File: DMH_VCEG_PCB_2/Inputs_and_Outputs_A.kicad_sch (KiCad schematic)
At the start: 35 parts, among them J1 TS_Jack_6.35mm_Sw, J10 TS_Jack_6.35mm_Sw, J2 TS_Jack_6.35mm_Sw, J200 IDC_02x08, J21 Conn_01x10_PinHeader, J22 Conn_01x10_PinHeader, J23 Conn_01x10_PinHeader, J27 Conn_01x06_PinHeader, J3 TS_Jack_6.35mm_Sw, J4 TS_Jack_6.35mm_Sw, J5 TS_Jack_6.35mm_Sw, J6 TS_Jack_6.35mm_Sw, J7 TS_Jack_6.35mm_Sw, J8 TS_Jack_6.35mm_Sw, J9 TS_Jack_6.35mm_Sw, U21 TL072, U9 TL074

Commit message: Placed ICs and pin headers on PCB 2
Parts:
- J21, J22, J23: footprint Connector_PinHeader_2.54mm:PinHeader_1x10_P2.54mm_Vertical -> Connector_PinSocket_2.54mm:PinSocket_1x10_P2.54mm_Vertical
- J27: footprint Connector_PinHeader_2.54mm:PinHeader_1x06_P2.54mm_Vertical -> Connector_PinSocket_2.54mm:PinSocket_1x06_P2.54mm_Vertical
- J27: footprint (none) -> Connector_PinSocket_2.54mm:PinSocket_1x06_P2.54mm_Vertical
- U21: footprint Package_DIP:DIP-8_W7.62mm -> Package_DIP:DIP-8_W7.62mm_Socket
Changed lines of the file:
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@@
 			)
 		)
-		(property "Footprint" "Connector_PinHeader_2.54mm:PinHeader_1x10_P2.54mm_Vertical"
+		(property "Footprint" "Connector_PinSocket_2.54mm:PinSocket_1x10_P2.54mm_Vertical"
 			(at 146.05 124.46 0)
 			(effects
@@
 			)
 		)
-		(property "Footprint" "Connector_PinHeader_2.54mm:PinHeader_1x10_P2.54mm_Vertical"
+		(property "Footprint" "Connector_PinSocket_2.54mm:PinSocket_1x10_P2.54mm_Vertical"
 			(at 190.5 179.07 0)
 			(effects
@@
 			)
 		)
-		(property "Footprint" "Connector_PinHeader_2.54mm:PinHeader_1x10_P2.54mm_Vertical"
+		(property "Footprint" "Connector_PinSocket_2.54mm:PinSocket_1x10_P2.54mm_Vertical"
 			(at 146.05 29.21 0)
 			(effects
@@
 			)
 		)
-		(property "Footprint" "Connector_PinHeader_2.54mm:PinHeader_1x10_P2.54mm_Vertical"
+		(property "Footprint" "Connector_PinSocket_2.54mm:PinSocket_1x10_P2.54mm_Vertical"
 			(at 190.5 163.83 0)
 			(effects
@@
 			)
 		)
-		(property "Footprint" "Connector_PinHeader_2.54mm:PinHeader_1x06_P2.54mm_Vertical"
+		(property "Footprint" "Connector_PinSocket_2.54mm:PinSocket_1x06_P2.54mm_Vertical"
 			(at 107.95 223.52 0)
 			(effects
@@
 			)
 		)
-		(property "Footprint" "Connector_PinHeader_2.54mm:PinHeader_1x10_P2.54mm_Vertical"
+		(property "Footprint" "Connector_PinSocket_2.54mm:PinSocket_1x10_P2.54mm_Vertical"
 			(at 190.5 151.13 0)
 			(effects
@@
 			)
 		)
-		(property "Footprint" "Connector_PinHeader_2.54mm:PinHeader_1x10_P2.54mm_Vertical"
+		(property "Footprint" "Connector_PinSocket_2.54mm:PinSocket_1x10_P2.54mm_Vertical"
 			(at 88.9 90.17 0)
 			(effects
@@
 			)
 		)
-		(property "Footprint" ""
+		(property "Footprint" "Connector_PinSocket_2.54mm:PinSocket_1x06_P2.54mm_Vertical"
 			(at 190.5 189.23 0)
 			(effects
@@
 			)
 		)
-		(property "Footprint" "Connector_PinHeader_2.54mm:PinHeader_1x10_P2.54mm_Vertical"
+		(property "Footprint" "Connector_PinSocket_2.54mm:PinSocket_1x10_P2.54mm_Vertical"
 			(at 190.5 176.53 0)
 			(effects
@@
 			)
 		)
-		(property "Footprint" "Connector_PinHeader_2.54mm:PinHeader_1x06_P2.54mm_Vertical"
+		(property "Footprint" "Connector_PinSocket_2.54mm:PinSocket_1x06_P2.54mm_Vertical"
 			(at 177.8 220.98 0)
 			(effects
@@
 			)
 		)
-		(property "Footprint" "Connector_PinHeader_2.54mm:PinHeader_1x10_P2.54mm_Vertical"
+		(property "Footprint" "Connector_PinSocket_2.54mm:PinSocket_1x10_P2.54mm_Vertical"
 			(at 88.9 58.42 0)
 			(effects
@@
 			)
 		)
-		(property "Footprint" "Connector_PinHeader_2.54mm:PinHeader_1x10_P2.54mm_Vertical"
+		(property "Footprint" "Connector_PinSocket_2.54mm:PinSocket_1x10_P2.54mm_Vertical"
 			(at 88.9 121.92 0)
 			(effects
@@
 			)
 		)
-		(property "Footprint" "Connector_PinHeader_2.54mm:PinHeader_1x10_P2.54mm_Vertical"
+		(property "Footprint" "Connector_PinSocket_2.54mm:PinSocket_1x10_P2.54mm_Vertical"
 			(at 88.9 26.67 0)
 			(effects
@@
 			)
 		)
-		(property "Footprint" "Connector_PinHeader_2.54mm:PinHeader_1x10_P2.54mm_Vertical"
+		(property "Footprint" "Connector_PinSocket_2.54mm:PinSocket_1x10_P2.54mm_Vertical"
 			(at 146.05 60.96 0)
 			(effects
@@
 			)
 		)
-		(property "Footprint" "Connector_PinHeader_2.54mm:PinHeader_1x10_P2.54mm_Vertical"
+		(property "Footprint" "Connector_PinSocket_2.54mm:PinSocket_1x10_P2.54mm_Vertical"
 			(at 190.5 153.67 0)
 			(effects
@@
 			)
 		)
-		(property "Footprint" ""
+		(property "Footprint" "Connector_PinSocket_2.54mm:PinSocket_1x06_P2.54mm_Vertical"
 			(at 190.5 191.77 0)
 			(effects
@@
 			)
 		)
-		(property "Footprint" "Connector_PinHeader_2.54mm:PinHeader_1x10_P2.54mm_Vertical"
+		(property "Footprint" "Connector_PinSocket_2.54mm:PinSocket_1x10_P2.54mm_Vertical"
 			(at 146.05 92.71 0)
 			(effects
@@
 			)
 		)
-		(property "Footprint" "Package_DIP:DIP-8_W7.62mm"
+		(property "Footprint" "Package_DIP:DIP-8_W7.62mm_Socket"
 			(at 146.05 228.6 0)
 			(effects
@@
 			)
 		)
-		(property "Footprint" "Connector_PinHeader_2.54mm:PinHeader_1x10_P2.54mm_Vertical"
+		(property "Footprint" "Connector_PinSocket_2.54mm:PinSocket_1x10_P2.54mm_Vertical"
 			(at 190.5 166.37 0)
 			(effects

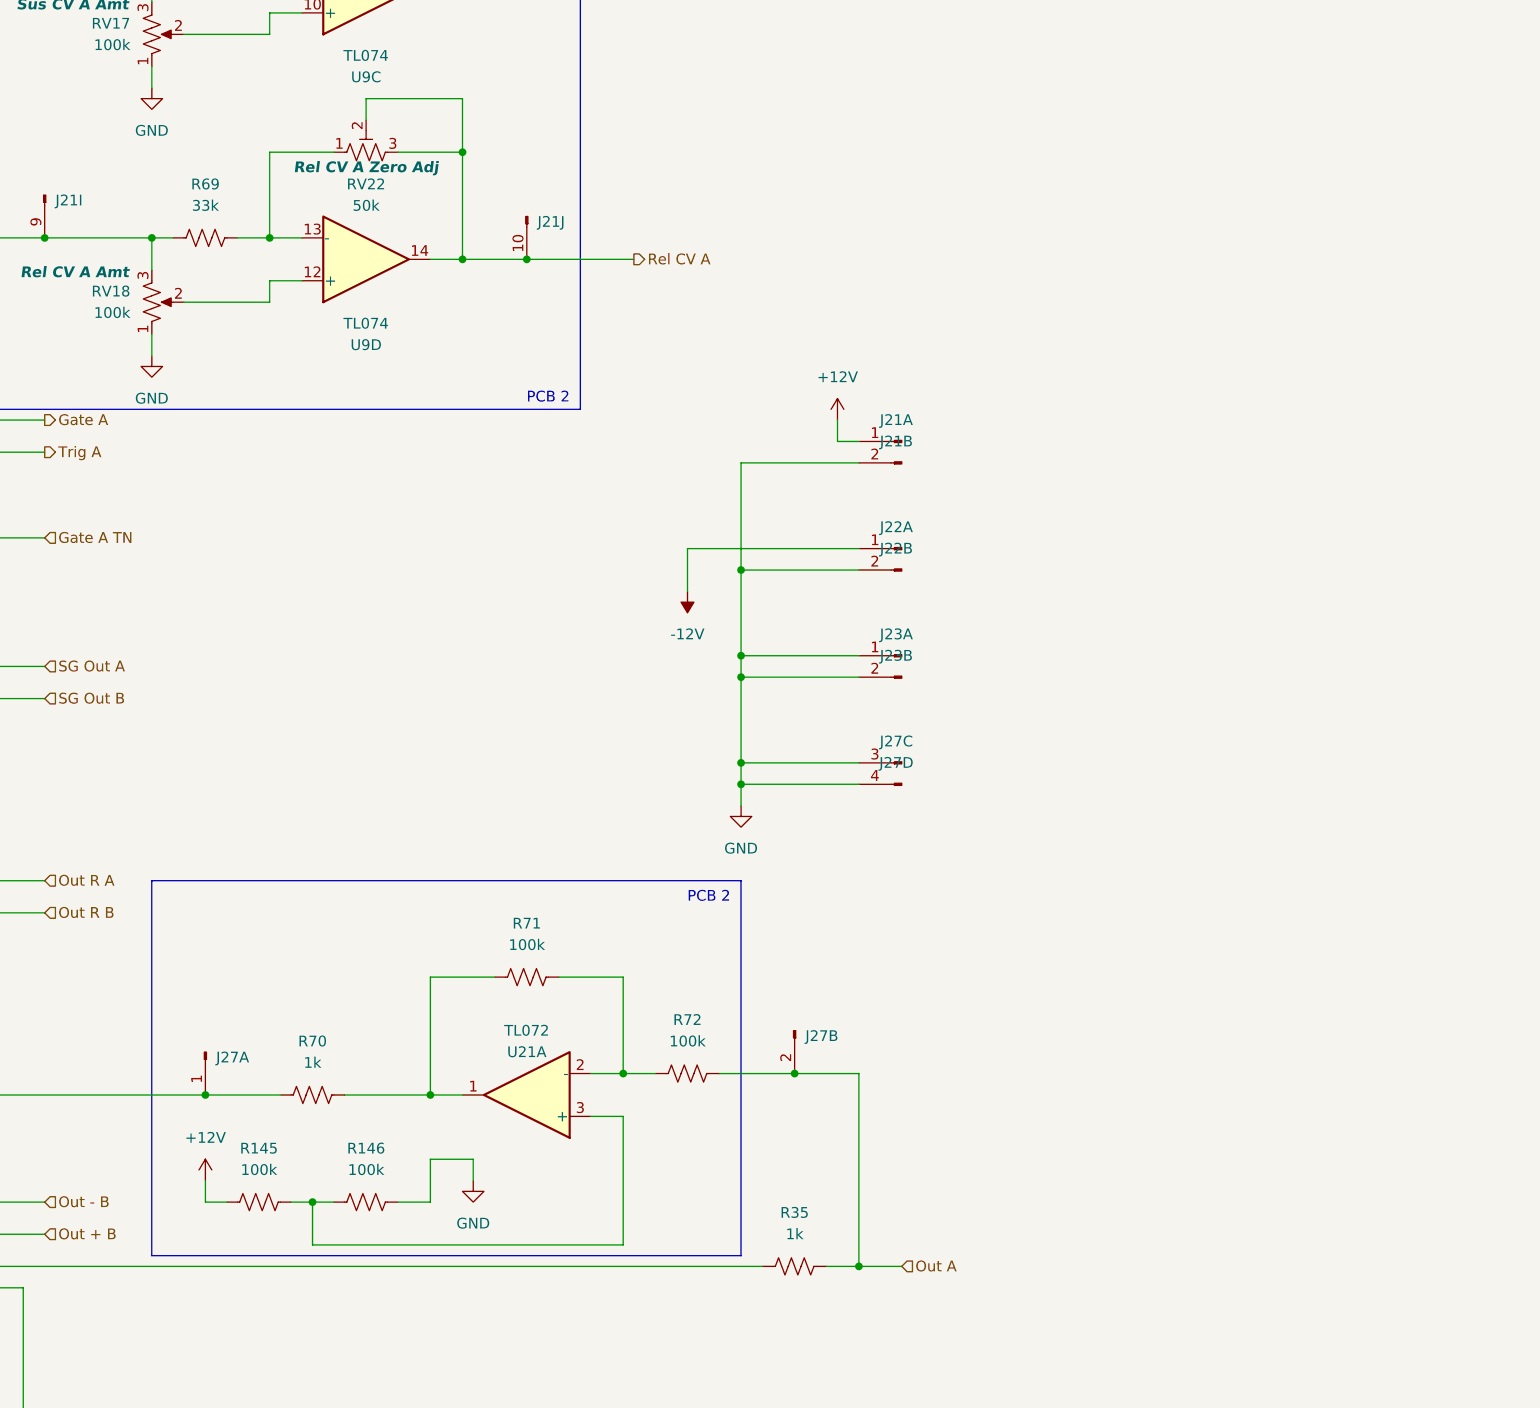
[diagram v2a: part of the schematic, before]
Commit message: Addition of manual gate ongoing
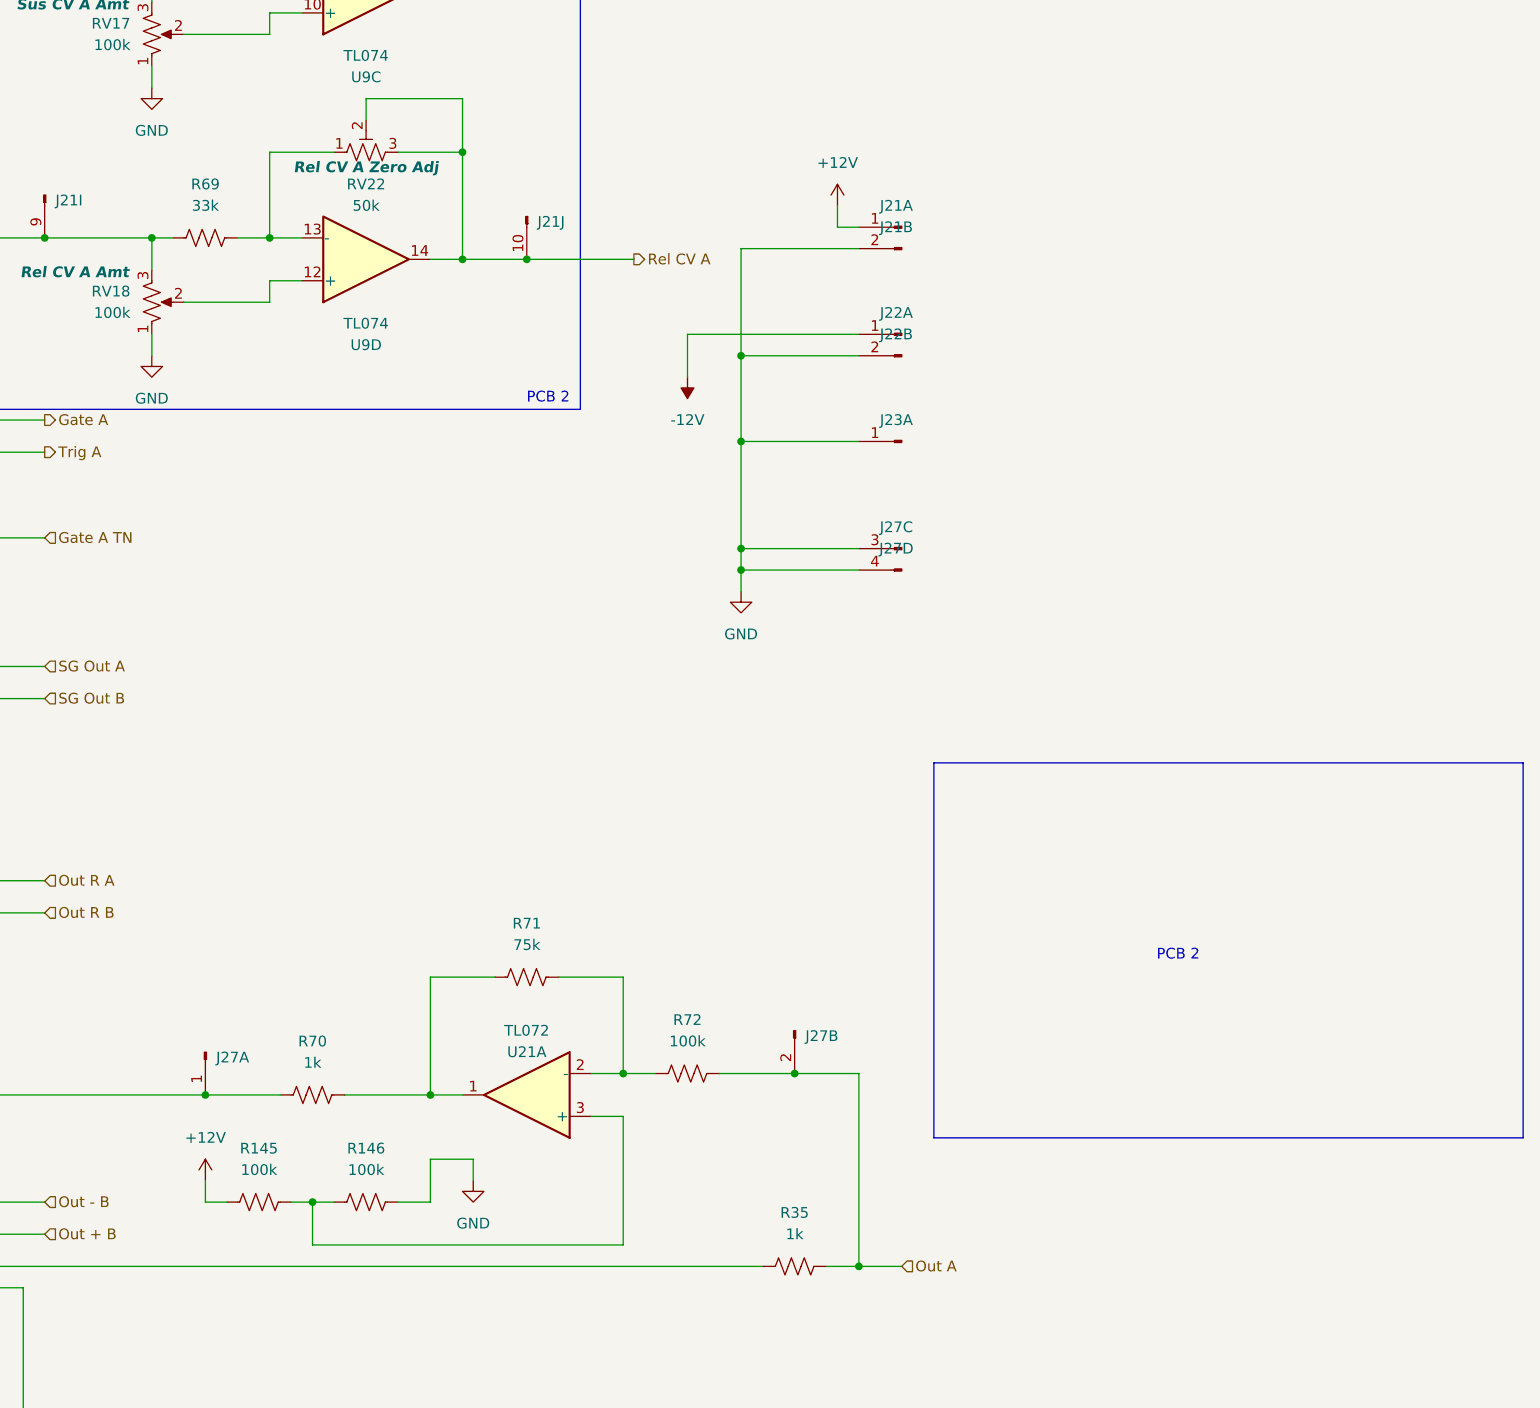
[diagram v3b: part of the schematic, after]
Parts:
- removed unit 2 of J23
- R71: value 100k -> 75k
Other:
- moved on the sheet: J21A, J21B, J22A, J22B, J23A, J27C, J27D
